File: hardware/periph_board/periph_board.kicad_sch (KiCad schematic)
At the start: 42 parts, among them IC100 CD74HC4067SM96, IC101 LM2937ET-3.3_NOPB, IC102 MCP3221AxT-E_OT, J100 2x8 Socket Pins, J101 2x8 Plug Pins

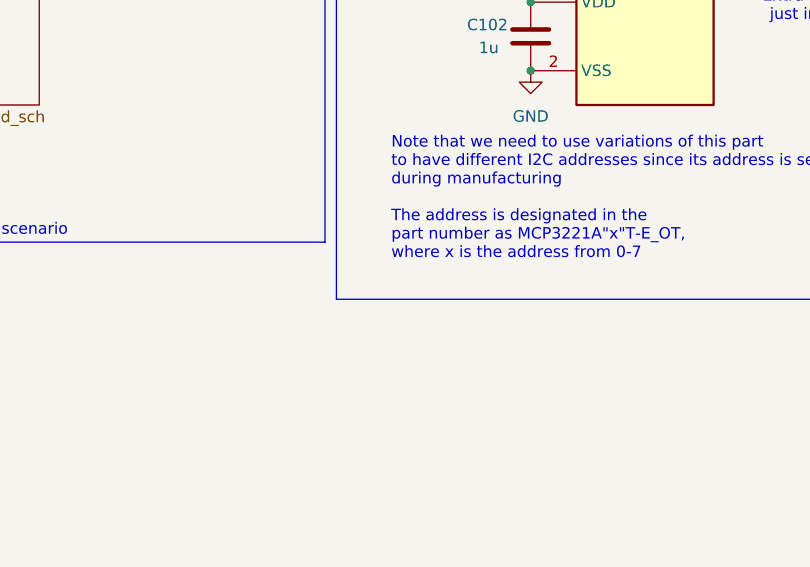
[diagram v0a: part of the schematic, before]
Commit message: main board stuff. removed usbc for power. added level shifter for led logic signal. added lights for mux select signals. finished layout + pass DRC
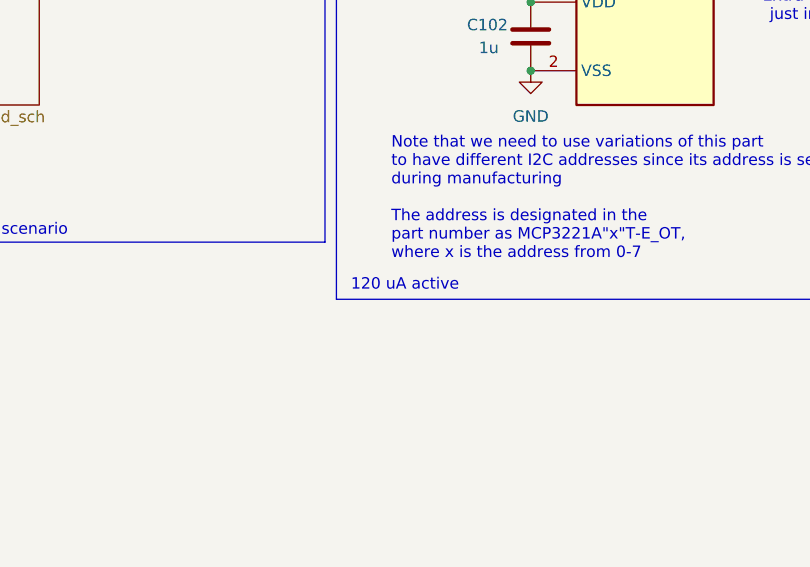
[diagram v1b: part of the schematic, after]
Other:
- note added: "120 uA active"
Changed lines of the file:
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@@
+		)
+	)
+	(text "120 uA active"
+		(exclude_from_sim no)
+		(at 110.49 101.346 0)
+		(effects
+			(font
+				(size 1.27 1.27)
+			)
 		)
 	)
